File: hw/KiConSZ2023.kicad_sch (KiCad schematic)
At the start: 2 parts

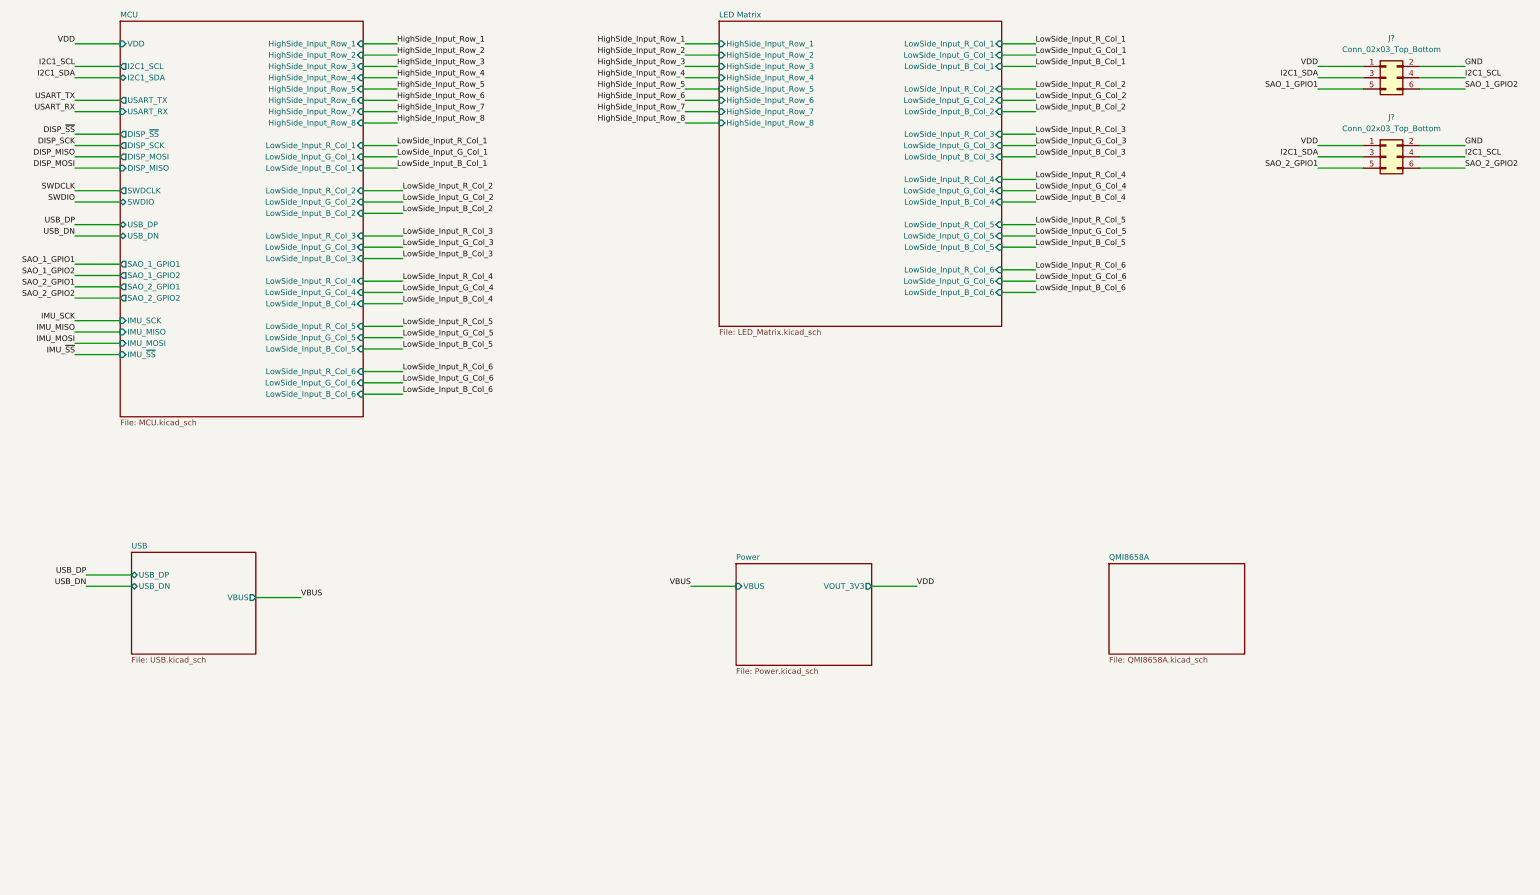
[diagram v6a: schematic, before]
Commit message: updated and fix ERCs
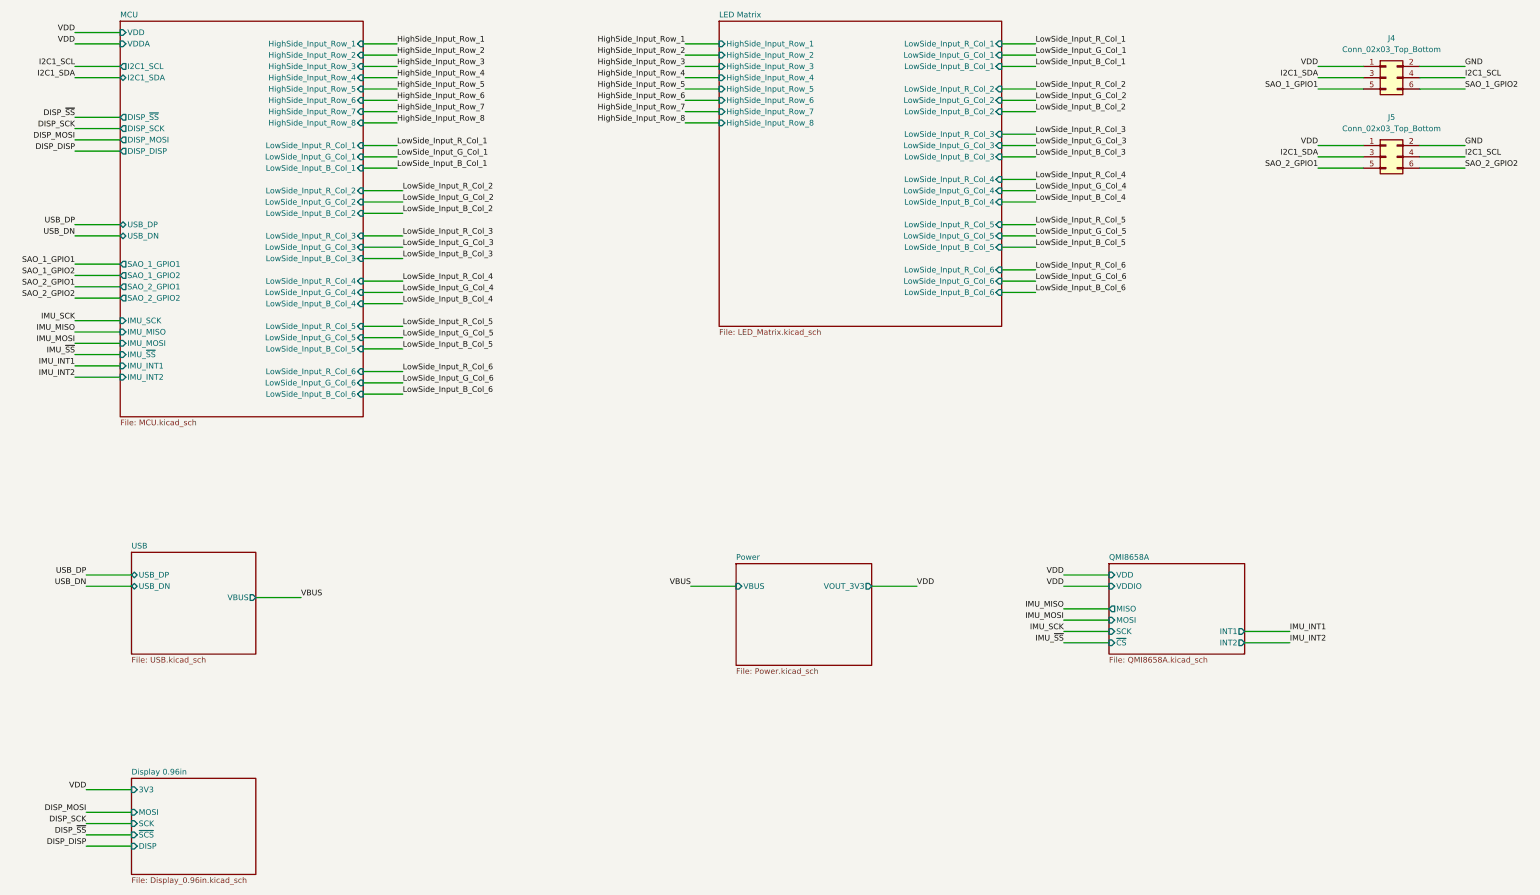
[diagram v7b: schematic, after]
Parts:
- gave numbers to parts that had none: 2
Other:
- added sheet Display 0.96in (Display_0.96in.kicad_sch)
- sheet MCU ports: added DISP_DISP, IMU_INT1, IMU_INT2, VDDA; removed DISP_MISO, SWDCLK, SWDIO, USART_RX, USART_TX
- sheet QMI8658A ports: added INT1, INT2, MISO, MOSI, SCK, VDD, VDDIO, ~{CS}; removed none

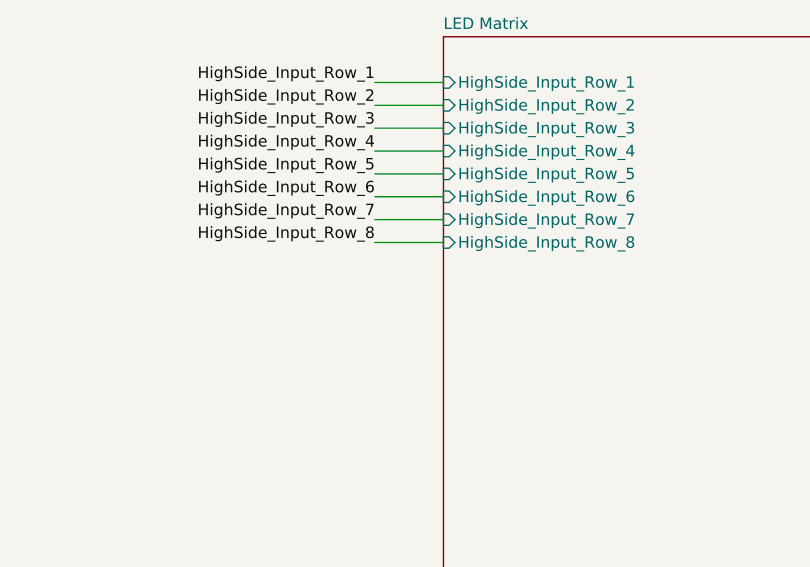
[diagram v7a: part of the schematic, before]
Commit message: added VDD for NMOS matrix
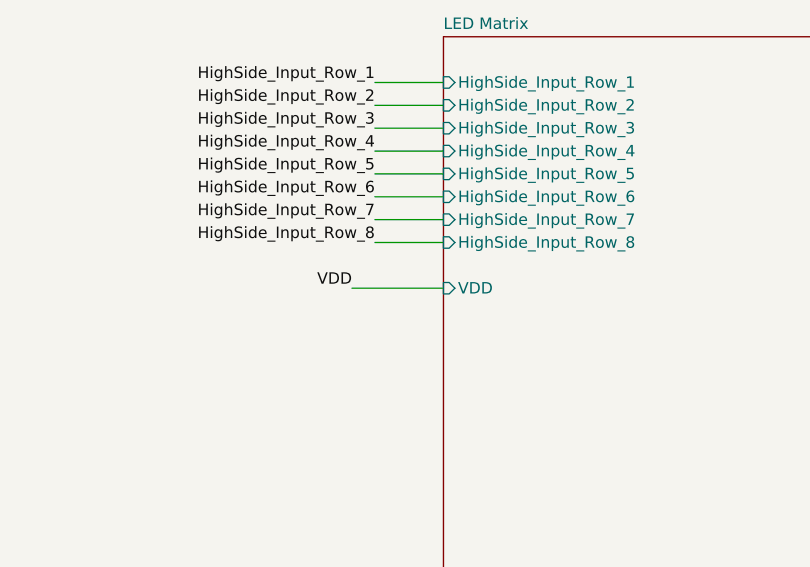
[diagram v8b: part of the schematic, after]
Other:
- sheet LED Matrix ports: added VDD; removed none
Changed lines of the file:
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@@
+    (stroke (width 0) (type default))
+  )
+  (wire (pts (xy 177.8 76.2) (xy 167.64 76.2))
     (stroke (width 0) (type default))
   )
@@
   (label "LowSide_Input_B_Col_6" (at 248.92 109.22 0) (fields_autoplaced)
     (effects (font (size 1.27 1.27)) (justify left bottom))
+  )
+  (label "VDD" (at 167.64 76.2 180) (fields_autoplaced)
+    (effects (font (size 1.27 1.27)) (justify right bottom))
   )
   (label "DISP_SCK" (at 35.56 228.6 180) (fields_autoplaced)
@@
       (effects (font (size 1.27 1.27)) (justify right))
     )
+    (pin "VDD" input (at 177.8 76.2 180)
+      (effects (font (size 1.27 1.27)) (justify left))
+    )
     (instances
